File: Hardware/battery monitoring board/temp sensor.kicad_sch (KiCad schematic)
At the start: 18 parts, among them J4 Conn_01x02, U1 MAX31855KASA

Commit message: erc-clear battery board
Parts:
- J4: footprint 4ms_Connector:Pins_1x02_2.54mm_TH -> Library:TE_282836-2
- renumbered TP10 to cs_t, TP11 to sck, TP9 to so
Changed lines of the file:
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@@
   (symbol (lib_id "Connector:TestPoint") (at 166.1092 96.266 0) (unit 1)
     (in_bom yes) (on_board yes) (dnp no)
-    (property "Reference" "TP9" (at 161.29 90.17 0)
+    (property "Reference" "so" (at 161.29 90.17 0)
       (effects (font (size 1.27 1.27)) (justify left))
     )
@@
       (project "battery monitoring board"
         (path "/bf623d80-ca5a-491f-9daa-4dffbeba5279/5ec2dbdf-a276-4d4c-99fc-008475c1e770"
-          (reference "TP9") (unit 1)
+          (reference "so") (unit 1)
         )
       )
@@
   (symbol (lib_id "Connector:TestPoint") (at 168.2309 101.346 180) (unit 1)
     (in_bom yes) (on_board yes) (dnp no)
-    (property "Reference" "TP10" (at 166.37 106.68 0)
+    (property "Reference" "cs_t" (at 166.37 106.68 0)
       (effects (font (size 1.27 1.27)) (justify right))
     )
@@
       (project "battery monitoring board"
         (path "/bf623d80-ca5a-491f-9daa-4dffbeba5279/5ec2dbdf-a276-4d4c-99fc-008475c1e770"
-          (reference "TP10") (unit 1)
+          (reference "cs_t") (unit 1)
         )
       )
@@
   (symbol (lib_id "Connector:TestPoint") (at 168.2646 93.726 0) (unit 1)
     (in_bom yes) (on_board yes) (dnp no)
-    (property "Reference" "TP11" (at 166.37 86.36 0)
+    (property "Reference" "sck" (at 166.37 86.36 0)
       (effects (font (size 1.27 1.27)) (justify left))
     )
@@
       (project "battery monitoring board"
         (path "/bf623d80-ca5a-491f-9daa-4dffbeba5279/5ec2dbdf-a276-4d4c-99fc-008475c1e770"
-          (reference "TP11") (unit 1)
+          (reference "sck") (unit 1)
         )
       )
@@
       (effects (font (size 1.27 1.27)))
     )
-    (property "Footprint" "4ms_Connector:Pins_1x02_2.54mm_TH" (at 56.769 106.045 0)
-      (effects (font (size 1.27 1.27)) hide)
-    )
+    (property "Footprint" "Library:TE_282836-2" (at 56.769 106.045 0)
+      (effects (font (size 1.27 1.27)) hide)
+    )

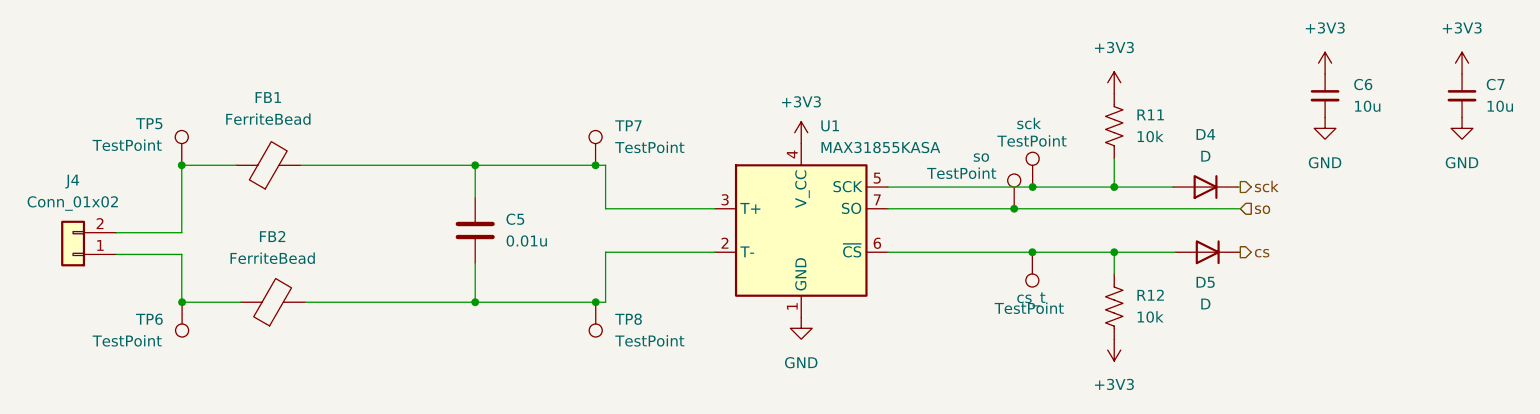
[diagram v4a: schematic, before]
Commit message: updated battery pcb (voltage dividers etc)
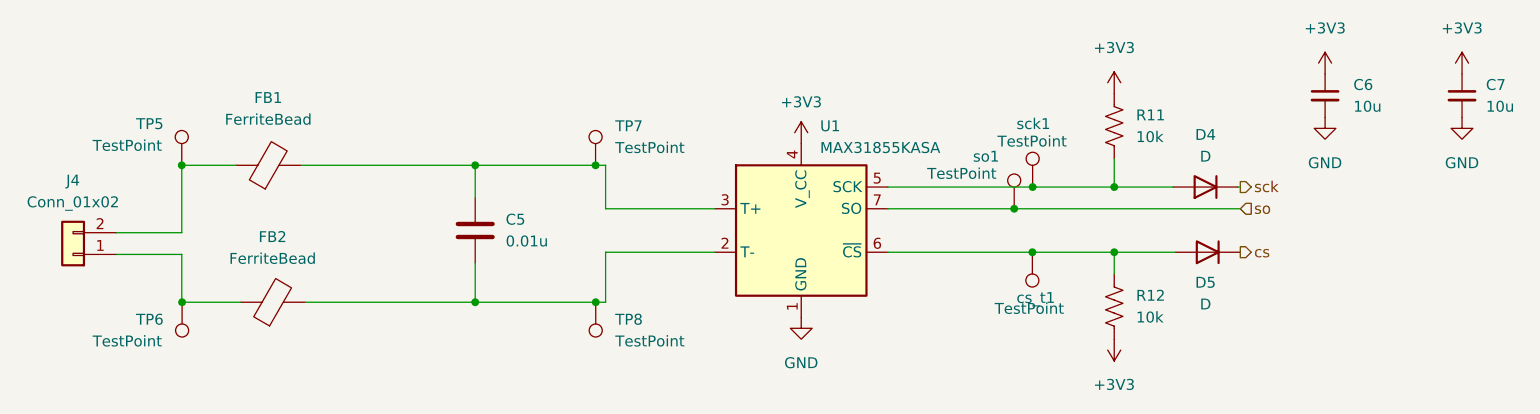
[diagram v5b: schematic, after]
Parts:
- renumbered cs_t to cs_t1, sck to sck1, so to so1
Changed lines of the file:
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@@
   (symbol (lib_id "Connector:TestPoint") (at 166.1092 96.266 0) (unit 1)
     (in_bom yes) (on_board yes) (dnp no)
-    (property "Reference" "so" (at 161.29 90.17 0)
+    (property "Reference" "so1" (at 161.29 90.17 0)
       (effects (font (size 1.27 1.27)) (justify left))
     )
@@
       (project "battery monitoring board"
         (path "/bf623d80-ca5a-491f-9daa-4dffbeba5279/5ec2dbdf-a276-4d4c-99fc-008475c1e770"
-          (reference "so") (unit 1)
+          (reference "so1") (unit 1)
         )
       )
@@
   (symbol (lib_id "Connector:TestPoint") (at 168.2309 101.346 180) (unit 1)
     (in_bom yes) (on_board yes) (dnp no)
-    (property "Reference" "cs_t" (at 166.37 106.68 0)
+    (property "Reference" "cs_t1" (at 166.37 106.68 0)
       (effects (font (size 1.27 1.27)) (justify right))
     )
@@
       (project "battery monitoring board"
         (path "/bf623d80-ca5a-491f-9daa-4dffbeba5279/5ec2dbdf-a276-4d4c-99fc-008475c1e770"
-          (reference "cs_t") (unit 1)
+          (reference "cs_t1") (unit 1)
         )
       )
@@
   (symbol (lib_id "Connector:TestPoint") (at 168.2646 93.726 0) (unit 1)
     (in_bom yes) (on_board yes) (dnp no)
-    (property "Reference" "sck" (at 166.37 86.36 0)
+    (property "Reference" "sck1" (at 166.37 86.36 0)
       (effects (font (size 1.27 1.27)) (justify left))
     )
@@
       (project "battery monitoring board"
         (path "/bf623d80-ca5a-491f-9daa-4dffbeba5279/5ec2dbdf-a276-4d4c-99fc-008475c1e770"
-          (reference "sck") (unit 1)
-        )
-      )
+          (reference "sck1") (unit 1)
+        )
+      )

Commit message: finalized battery board !!
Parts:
- removed TP5, TP6, TP7, TP8: TestPoint, PCM_4ms_TestPoint:TestPoint_Pad_06, symbol Connector:TestPoint
- renumbered C5 to C6, C6 to C7, C7 to C8, D5 to D3, R12 to R10
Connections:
- net cs: now also cs_t1.1
- net sck: now also sck1.1
- net at D4.2 (A), R11.2, U1.5 (SCK): no longer sck1.1
- net at D3.2 (A), R10.1, U1.6 (~{CS}): no longer cs_t1.1
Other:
- moved on the sheet: D3, D4, R10, R11
